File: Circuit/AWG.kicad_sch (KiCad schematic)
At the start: 19 parts, among them J1 Power, J2 Pump 1, J3 Pump 2, J4 Pump 3, J5 WL1, J6 Display, M1 Fan_3pin, M2 Fan_3pin, Q1 RFP30N06LE, Q2 RFP30N06LE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

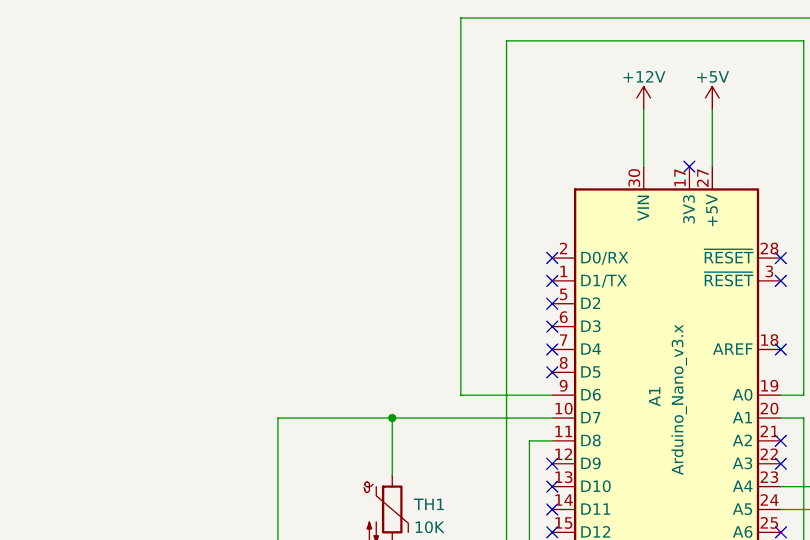
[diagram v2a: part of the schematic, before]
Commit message: [Circuit][Code] Add a DHT module to measure environment temperature and humidity
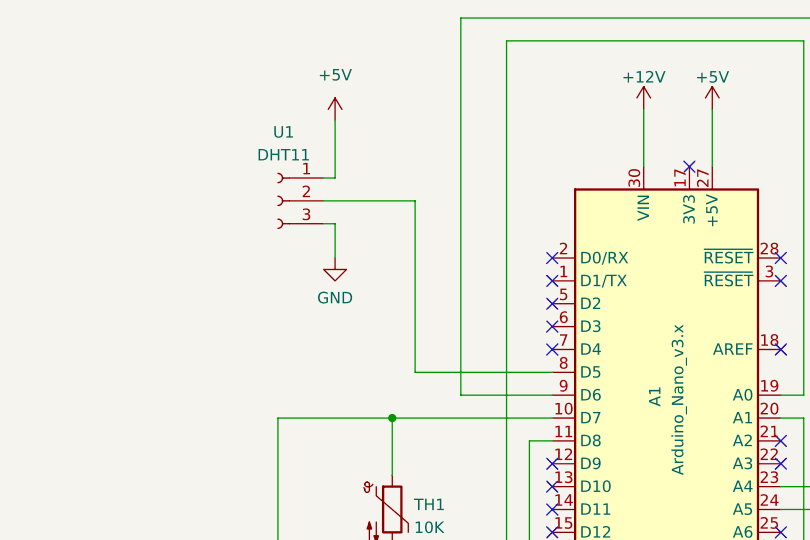
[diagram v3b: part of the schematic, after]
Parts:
- added U1: DHT11, Connector_PinSocket_2.54mm:PinSocket_1x03_P2.54mm_Vertical, symbol Connector:Conn_01x03_Female
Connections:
- net +5V: now also U1.1 (Pin_1)
- net GND: now also U1.3 (Pin_3)
- net at A1.8 (D5): now also U1.2 (Pin_2)
- no-connect marks 21 -> 20
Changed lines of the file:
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@@
   (no_connect (at 162.56 73.66))
   (no_connect (at 162.56 76.2))
-  (no_connect (at 162.56 78.74))
   (no_connect (at 162.56 68.58))
   (no_connect (at 162.56 96.52))
@@
     (stroke (width 0) (type default) (color 0 0 0 0))
   )
+  (wire (pts (xy 137.16 62.23) (xy 138.43 62.23))
+    (stroke (width 0) (type default) (color 0 0 0 0))
+  )
   (wire (pts (xy 49.53 54.61) (xy 57.15 54.61))
     (stroke (width 0) (type default) (color 0 0 0 0))
@@
     (stroke (width 0) (type default) (color 0 0 0 0))
   )
+  (wire (pts (xy 138.43 50.8) (xy 138.43 57.15))
+    (stroke (width 0) (type default) (color 0 0 0 0))
+  )
+  (wire (pts (xy 147.32 59.69) (xy 147.32 78.74))
+    (stroke (width 0) (type default) (color 0 0 0 0))
+  )
   (wire (pts (xy 74.93 123.19) (xy 74.93 134.62))
     (stroke (width 0) (type default) (color 0 0 0 0))
@@
     (stroke (width 0) (type default) (color 0 0 0 0))
   )
+  (wire (pts (xy 137.16 57.15) (xy 138.43 57.15))
+    (stroke (width 0) (type default) (color 0 0 0 0))
+  )
   (wire (pts (xy 39.37 123.19) (xy 54.61 123.19))
     (stroke (width 0) (type default) (color 0 0 0 0))
@@
     (stroke (width 0) (type default) (color 0 0 0 0))
   )
+  (wire (pts (xy 137.16 59.69) (xy 147.32 59.69))
+    (stroke (width 0) (type default) (color 0 0 0 0))
+  )
+  (wire (pts (xy 138.43 62.23) (xy 138.43 66.04))
+    (stroke (width 0) (type default) (color 0 0 0 0))
+  )
   (wire (pts (xy 54.61 72.39) (xy 49.53 72.39))
     (stroke (width 0) (type default) (color 0 0 0 0))
@@
   )
   (wire (pts (xy 217.17 157.48) (xy 217.17 154.94))
+    (stroke (width 0) (type default) (color 0 0 0 0))
+  )
+  (wire (pts (xy 162.56 78.74) (xy 147.32 78.74))
     (stroke (width 0) (type default) (color 0 0 0 0))
   )
@@
     (pin "1")
   )
+  (symbol (lib_id "power:+5V") (at 138.43 50.8 0) (unit 1)
+    (in_bom yes) (on_board yes) (fields_autoplaced)
+    (property "Reference" "#PWR?" (id 0) (at 138.43 54.61 0)
+      (effects (font (size 1.27 1.27)) hide)
+    )
+    (property "Value" "+5V" (id 1) (at 138.43 45.72 0))
+    (property "Footprint" "" (id 2) (at 138.43 50.8 0)
+      (effects (font (size 1.27 1.27)) hide)
+    )
+    (property "Datasheet" "" (id 3) (at 138.43 50.8 0)
+      (effects (font (size 1.27 1.27)) hide)
+    )
+    (pin "1")
+  )
   (symbol (lib_id "power:+12V") (at 74.93 120.65 0) (unit 1)
     (in_bom yes) (on_board yes) (fields_autoplaced)
@@
     )
     (property "Datasheet" "" (id 3) (at 227.33 68.58 0)
+      (effects (font (size 1.27 1.27)) hide)
+    )
+    (pin "1")
+  )
+  (symbol (lib_id "power:GND") (at 138.43 66.04 0) (unit 1)
+    (in_bom yes) (on_board yes) (fields_autoplaced)
+    (property "Reference" "#PWR?" (id 0) (at 138.43 72.39 0)
+      (effects (font (size 1.27 1.27)) hide)
+    )
+    (property "Value" "GND" (id 1) (at 138.43 70.4834 0))
+    (property "Footprint" "" (id 2) (at 138.43 66.04 0)
+      (effects (font (size 1.27 1.27)) hide)
+    )
+    (property "Datasheet" "" (id 3) (at 138.43 66.04 0)
       (effects (font (size 1.27 1.27)) hide)
     )
@@
     (pin "2")
   )
+  (symbol (lib_id "Connector:Conn_01x03_Female") (at 132.08 59.69 0) (mirror y) (unit 1)
+    (in_bom yes) (on_board yes) (fields_autoplaced)
+    (property "Reference" "U1" (id 0) (at 132.715 52.07 0))
+    (property "Value" "DHT11" (id 1) (at 132.715 54.61 0))
+    (property "Footprint" "Connector_PinSocket_2.54mm:PinSocket_1x03_P2.54mm_Vertical" (id 2) (at 132.08 59.69 0)
+      (effects (font (size 1.27 1.27)) hide)
+    )
+    (property "Datasheet" "~" (id 3) (at 132.08 59.69 0)
+      (effects (font (size 1.27 1.27)) hide)
+    )
+    (pin "1")
+    (pin "2")
+    (pin "3")
+  )
   (symbol (lib_id "power:GND") (at 144.78 121.92 0) (mirror y) (unit 1)
     (in_bom yes) (on_board yes)
@@
       (reference "#PWR?") (unit 1) (value "GND") (footprint "")
     )
+    (path "/0cec674f-f6a0-4bc7-b902-0893758fdb8b"
+      (reference "#PWR?") (unit 1) (value "+5V") (footprint "")
+    )
+    (path "/28b5f1b0-8e6e-4749-be9a-20b472aaafc5"
+      (reference "#PWR?") (unit 1) (value "GND") (footprint "")
+    )
     (path "/2bc11a90-ac28-40c7-8660-534c4fab6cc1"
       (reference "#PWR?") (unit 1) (value "GND") (footprint "")
@@
       (reference "TH1") (unit 1) (value "10K") (footprint "Connector_PinHeader_2.54mm:PinHeader_1x02_P2.54mm_Vertical")
     )
-  )
+    (path "/a4cdde95-b557-4573-83fe-761cd24d7a41"
+      (reference "U1") (unit 1) (value "DHT11") (footprint "Connector_PinSocket_2.54mm:PinSocket_1x03_P2.54mm_Vertical")
+    )
+  )

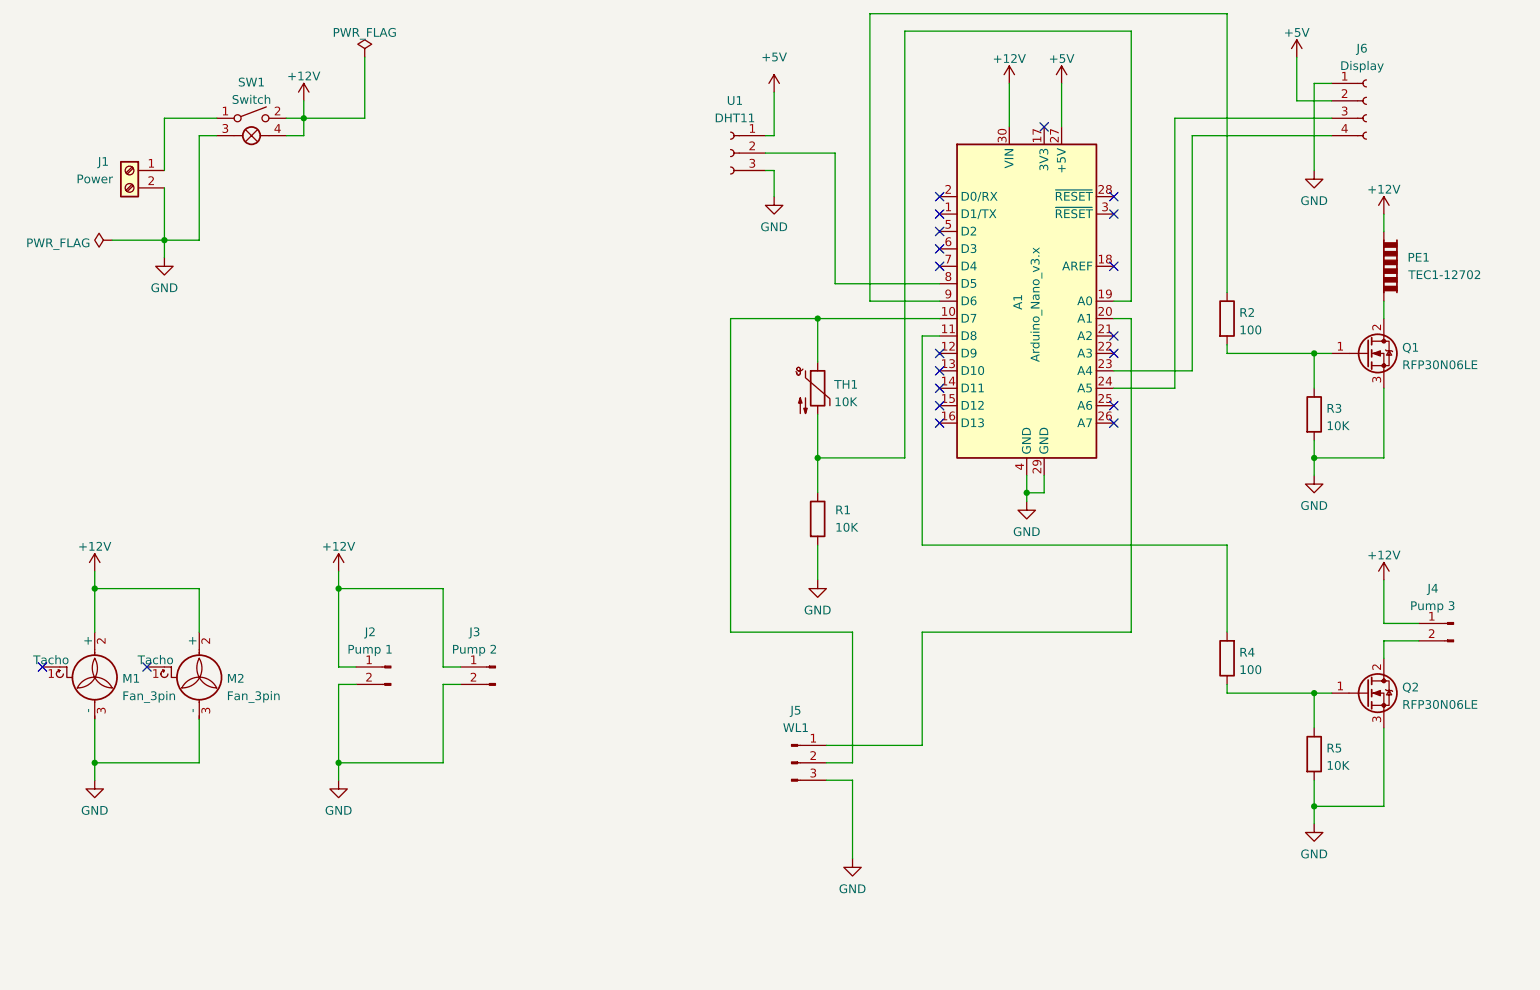
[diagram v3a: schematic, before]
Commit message: [Circuit] Adjust the GPIOs and design a PCB
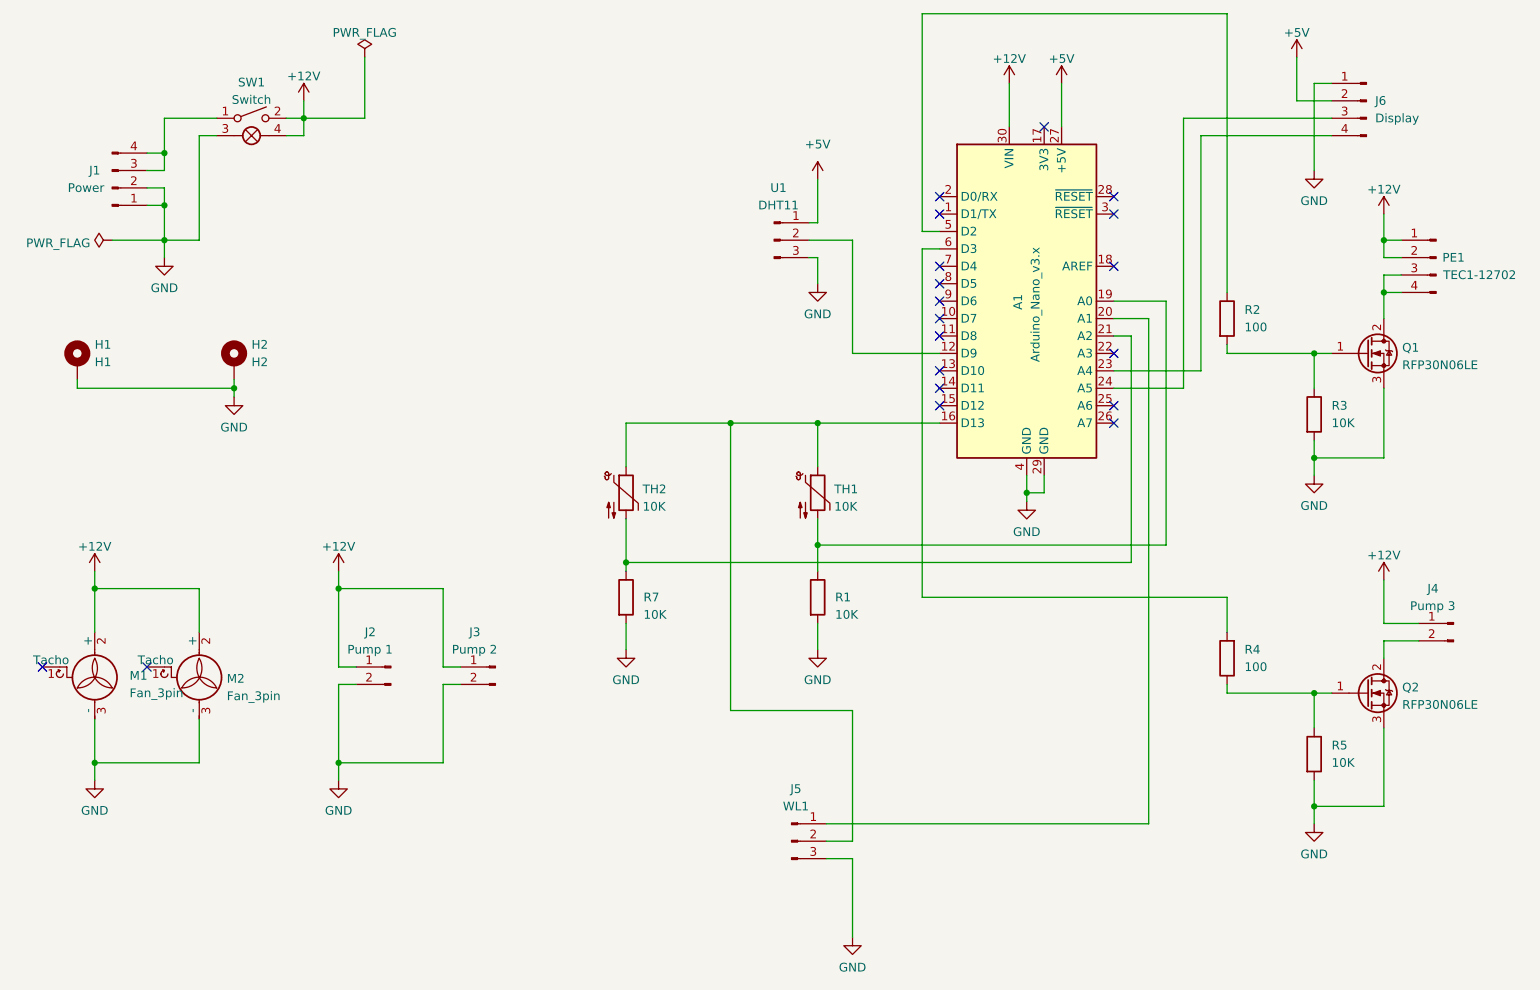
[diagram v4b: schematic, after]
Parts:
- removed J1: Power, TerminalBlock:TerminalBlock_bornier-2_P5.08mm, symbol Connector:Screw_Terminal_01x02
- added H1: H1, MountingHole:MountingHole_2.7mm_M2.5_Pad_Via, symbol Mechanical:MountingHole_Pad
- added H2: H2, MountingHole:MountingHole_2.7mm_M2.5_Pad_Via, symbol Mechanical:MountingHole_Pad
- added J1: Power, Connector_PinHeader_2.54mm:PinHeader_1x04_P2.54mm_Vertical, symbol Connector:Conn_01x04_Male
- added R7: 10K, Resistor_THT:R_Axial_DIN0207_L6.3mm_D2.5mm_P7.62mm_Horizontal, symbol Device:R
- added TH2: 10K, Connector_PinHeader_2.54mm:PinHeader_1x02_P2.54mm_Vertical, symbol Device:Thermistor_NTC
- J6: footprint Connector_PinSocket_2.54mm:PinSocket_1x04_P2.54mm_Vertical -> Connector_PinHeader_2.54mm:PinHeader_1x04_P2.54mm_Vertical; symbol Connector:Conn_01x04_Female -> Connector:Conn_01x04_Male
- PE1: footprint TerminalBlock:TerminalBlock_bornier-2_P5.08mm -> Connector_PinHeader_2.54mm:PinHeader_1x04_P2.54mm_Vertical; symbol Device:PeltierElement -> Connector:Conn_01x04_Male
- R1, R2, R3, R4, R5: footprint Resistor_THT:R_Axial_DIN0204_L3.6mm_D1.6mm_P7.62mm_Horizontal -> Resistor_THT:R_Axial_DIN0207_L6.3mm_D2.5mm_P7.62mm_Horizontal
- U1: footprint Connector_PinSocket_2.54mm:PinSocket_1x03_P2.54mm_Vertical -> Connector_PinHeader_2.54mm:PinHeader_1x03_P2.54mm_Vertical; symbol Connector:Conn_01x03_Female -> Connector:Conn_01x03_Male
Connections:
- net +12V: now also PE1.1 (Pin_1)
- net GND: now also H1.1, H2.1, J1.1 (Pin_1), J1.2 (Pin_2), R7.2
- net at J5.2 (Pin_2), TH1.1: now also A1.16 (D13), TH2.1; no longer A1.10 (D7)
- net at A1.11 (D8): no longer R4.2
- net at A1.12 (D9): now also U1.2 (Pin_2)
- net at A1.21 (A2): now also R7.1, TH2.2
- net at A1.5 (D2): now also R2.1
- net at A1.6 (D3): now also R4.2
- net at A1.8 (D5): no longer U1.2 (Pin_2)
- net at A1.9 (D6): no longer R2.1
- net at Q1.2 (D): now also PE1.3 (Pin_3), PE1.4 (Pin_4); no longer PE1.1
- net at SW1.1: now also J1.3 (Pin_3), J1.4 (Pin_4)
- no-connect marks 20 -> 19
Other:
- moved on the sheet: J5, R1, TH1
